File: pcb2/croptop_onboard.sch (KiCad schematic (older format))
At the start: 100 parts, among them J15 TSM-112-01-L-DV, J16 DM3D-SF, Q4 BSS138, Q5 BSS138, Q6 BSS138, SW2 SW_Push, SW3 SW_Push, SW4 SW_Push, U30 TPD4E1U06DBV, U31 TPD4E1U06DBV, U32 AP22802AW5, U33 AP22802AW5, U34 TPD4E1U06DBV, U35 TPD4E1U06DBV, U36 AP22802AW5, U37 TPD4E1U06DBV, U38 TPD4E1U06DBV, U39 LIS3DSHTR, U40 CAM-M8C-0, U41 Si7006-A20

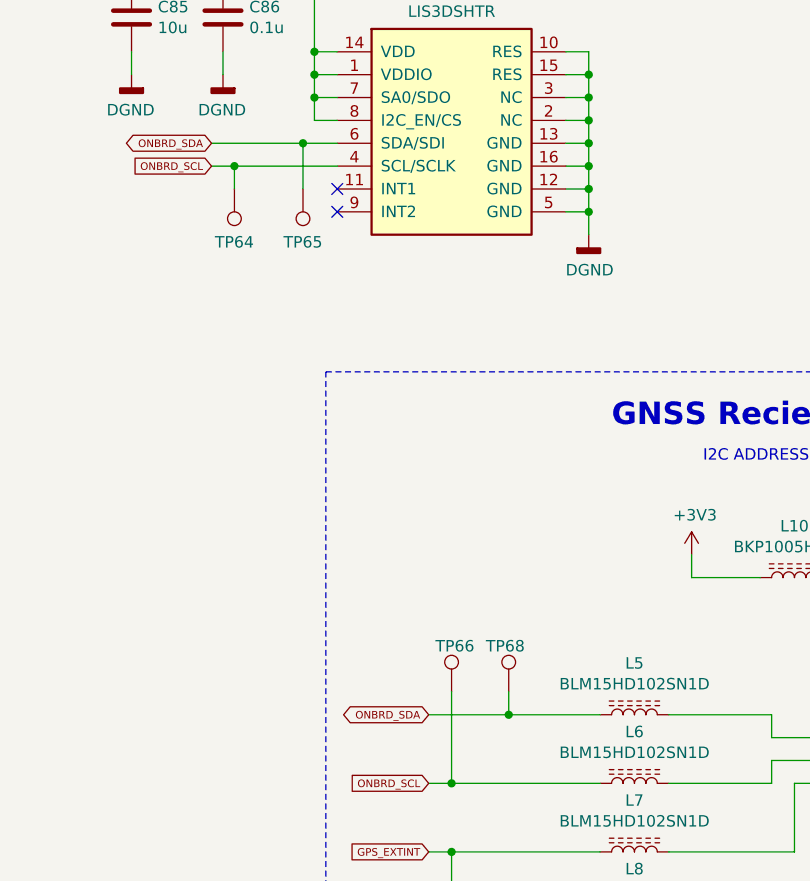
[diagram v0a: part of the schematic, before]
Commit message: Fixed Screen alignment
- Fixed pin alignment of LCD screen
- Pins now properly align with the ribbon cables of the LCD screen
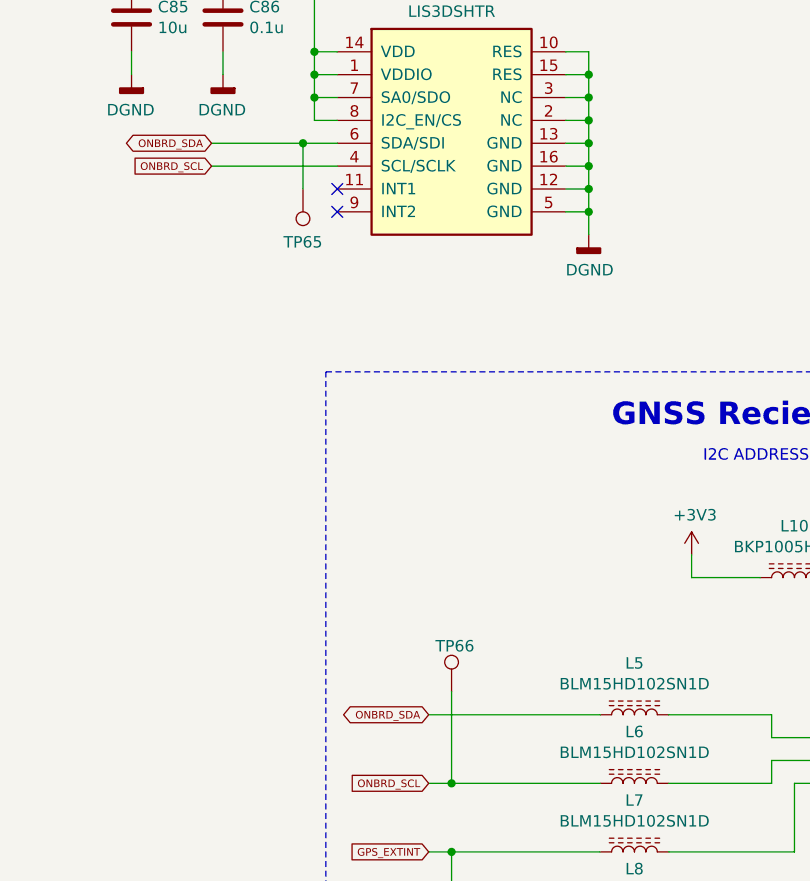
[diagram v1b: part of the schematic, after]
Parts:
- removed TP64, TP68: TestPoint, TestPoint:TestPoint_Pad_D1.0mm, symbol Connector:TestPoint
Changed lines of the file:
@@
 Wire Wire Line
 	13050 5650 13050 5750
-Wire Wire Line
-	9900 2450 10000 2450
 $Comp
 L Device:L_Core_Ferrite L8
@@
 Text GLabel 10850 5750 0    33   Input ~ 0
 ~GPS_RESET
-$Comp
-L Connector:TestPoint TP?
-U 1 1 60F3FF7D
-P 10000 2550
-AR Path="/64809F0C/60F3FF7D" Ref="TP?"  Part="1"
-AR Path="/66A12230/60F3FF7D" Ref="TP64"  Part="1"
-AR Path="/64807BBC/60F3FF7D" Ref="TP?"  Part="1"
-F 0 "TP64" H 10000 2783 50  0000 C CNN
-F 1 "TestPoint" H 10058 2579 50  0001 L CNN
-F 2 "TestPoint:TestPoint_Pad_D1.0mm" H 10200 2550 50  0001 C CNN
-F 3 "" H 10200 2550 50  0001 C CNN
-	1    10000 2550
-	-1   0    0    1
-$EndComp
-Wire Wire Line
-	10000 2550 10000 2450
 Wire Wire Line
 	10300 2550 10300 2350
@@
 NoConn ~ 10450 2550
 NoConn ~ 10450 2650
-Connection ~ 10000 2450
-Wire Wire Line
-	10000 2450 10450 2450
 Connection ~ 10300 2350
 Wire Wire Line
@@
 Wire Wire Line
 	12000 4250 12300 4250
-$Comp
-L Connector:TestPoint TP?
-U 1 1 5E9FCD1E
-P 11200 4750
-AR Path="/64809F0C/5E9FCD1E" Ref="TP?"  Part="1"
-AR Path="/66A12230/5E9FCD1E" Ref="TP68"  Part="1"
-AR Path="/64807BBC/5E9FCD1E" Ref="TP?"  Part="1"
-F 0 "TP68" H 11100 4950 50  0000 L CNN
-F 1 "TestPoint" H 11258 4779 50  0001 L CNN
-F 2 "TestPoint:TestPoint_Pad_D1.0mm" H 11400 4750 50  0001 C CNN
-F 3 "" H 11400 4750 50  0001 C CNN
-	1    11200 4750
-	1    0    0    -1
-$EndComp
 NoConn ~ 13150 4750
 NoConn ~ 13150 4850
@@
 	12650 5550 13150 5550
 Wire Wire Line
-	10850 4850 11200 4850
-Wire Wire Line
 	10850 5150 10950 5150
 Wire Wire Line
@@
 Wire Wire Line
 	10950 5150 11600 5150
-Wire Wire Line
-	11200 4750 11200 4850
-Connection ~ 11200 4850
-Wire Wire Line
-	11200 4850 11600 4850
 Wire Wire Line
 	11450 6050 11450 6150
@@
 	1    0    0    -1
 $EndComp
+Wire Wire Line
+	10850 4850 11600 4850
+Wire Wire Line
+	9900 2450 10450 2450
 $EndSCHEMATC
